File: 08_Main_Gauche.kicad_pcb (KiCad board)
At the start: 2 copper layers, 100 x 100 mm, 82 parts, among them J1 Conn_01x04, SW1 MX_1u, SW10 MX_1u, SW11 MX_1u, SW12 MX_1u, SW13 MX_1u, SW14 MX_1u, SW15 MX_1u, SW16 MX_1u, SW17 MX_1u, SW18 MX_1u, SW19 MX_1u, SW2 MX_1u, SW20 MX_1u, SW21 MX_1u, SW22 MX_1u, SW23 MX_1u, SW24 MX_1u, SW25 SW_Push, SW26 SW_Push, SW27 SW_Push, SW28 SW_Push, SW3 MX_1u, SW4 MX_1u, SW5 MX_1u, SW6 MX_1u, SW7 MX_1u, SW8 MX_1u, SW9 MX_1u, U1 MCP23017_SO

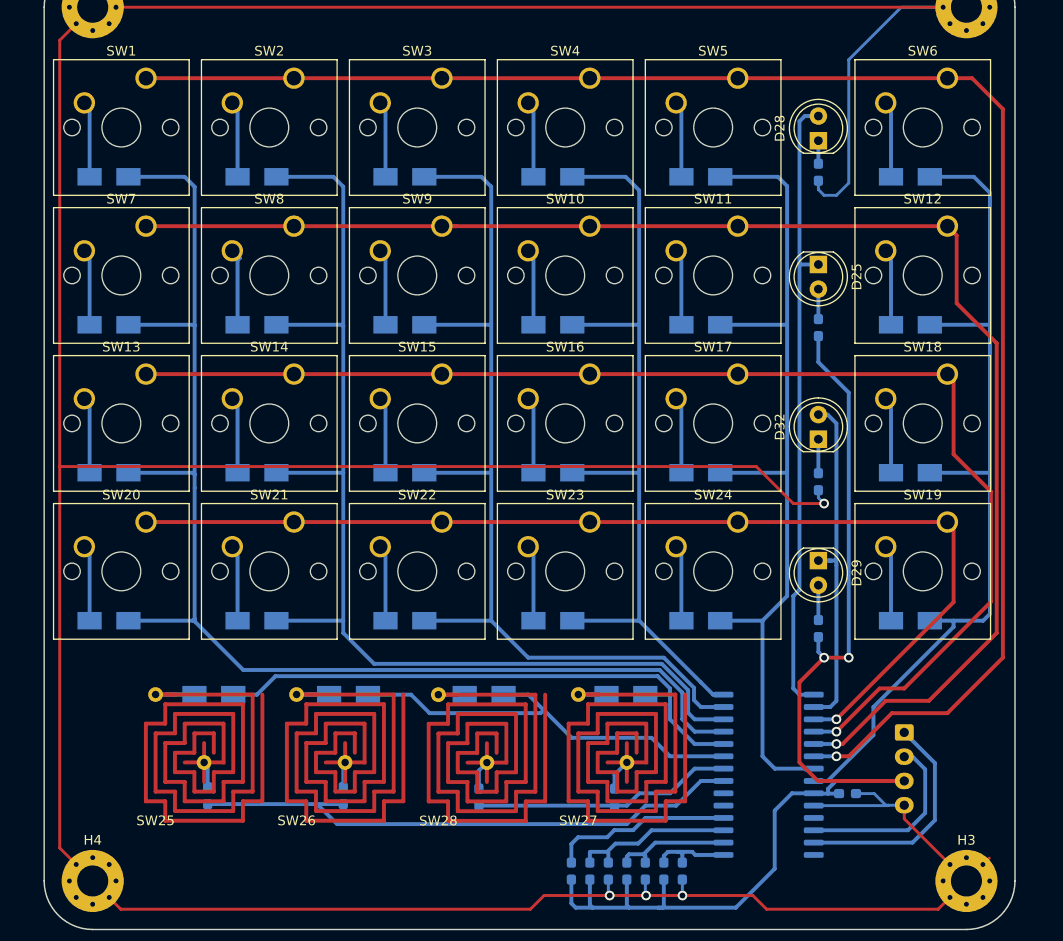
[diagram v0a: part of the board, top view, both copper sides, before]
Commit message: correction empreinte et routage; utilisation empreinte cherry mx led
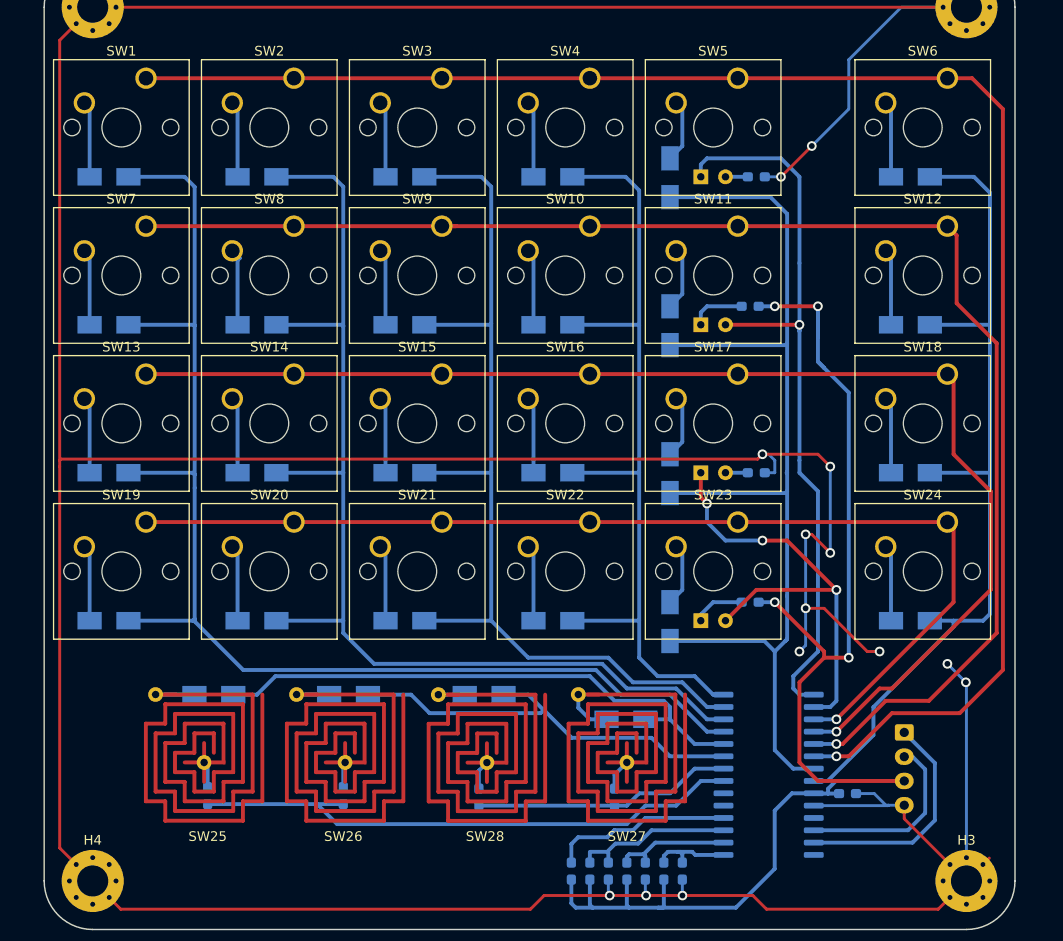
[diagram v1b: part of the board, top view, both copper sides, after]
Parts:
- removed D25, D28, D29, D32: LED, LED_THT:LED_D5.0mm
- removed the SW24 at (171.4, 113.0)
- added SW23: SW_Push_LED, Chimere:SW_MX_LED, F.Cu at (171.4, 113.0)
- SW11, SW17, SW5: value MX_1u -> SW_Push_LED; footprint Button_Switch_Keyboard:SW_Cherry_MX_1.00u_PCB -> Chimere:SW_MX_LED
- moved R7 7.54 mm to (172.7, 121.3), turned to 0 degrees
- moved R3 7.36 mm to (172.7, 90.8), turned to 0 degrees
- moved R9 6.46 mm to (173.4, 108.0), turned to 0 degrees
- moved R4 6.41 mm to (173.4, 77.5), turned to 0 degrees
- moved D11 3.18 mm to (164.5, 92.8), turned to 90 degrees
- moved D17 3.18 mm to (164.5, 108.0), turned to 90 degrees
- moved D23 3.18 mm to (164.5, 123.3), turned to 90 degrees
- moved D5 3.18 mm to (164.5, 77.6), turned to 90 degrees
- moved D30 2.54 mm to (159.9, 133.3)
- renumbered D20 to D19, D21 to D20, D22 to D21, D23 to D22, D24 to D23, D19 to D24, SW20 to SW19, SW21 to SW20, SW22 to SW21, SW23 to SW22, SW19 to SW24
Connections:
- R3 pad 1: Net-(D25-Pad2) -> Net-(R3-Pad1)
- R4 pad 1: Net-(D28-Pad1) -> Net-(R4-Pad1)
- R9 pad 1: Net-(D32-Pad1) -> Net-(R9-Pad1)
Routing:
- net GND: track 424.4 -> 482.8 mm, vias 4 -> 14
- net 3V3: track 119.5 -> 139.8 mm, vias 2 -> 4
- net COL1: track 91.0 -> 109.2 mm
- net LED1: track 35.7 -> 48.3 mm, vias 0 -> 3
- net LED0: track 65.2 -> 77.7 mm, vias 0 -> 1
- net Net-(R3-Pad1): track 0.00 -> 5.74 mm
- net Net-(D32-Pad1): track 3.50 -> 0.00 mm
- net Net-(D25-Pad2): track 3.08 -> 0.00 mm
- net Net-(D28-Pad1): track 2.38 -> 0.00 mm
- net Net-(R9-Pad1): track 0.00 -> 2.30 mm
- net Net-(R4-Pad1): track 0.00 -> 2.30 mm
- net COL2: track 84.4 -> 86.6 mm
- net Net-(D30-Pad2): track 2.91 -> 4.76 mm
- net Net-(R7-Pad1): track 3.58 -> 5.37 mm
- net COL5: track 133.4 -> 131.8 mm
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
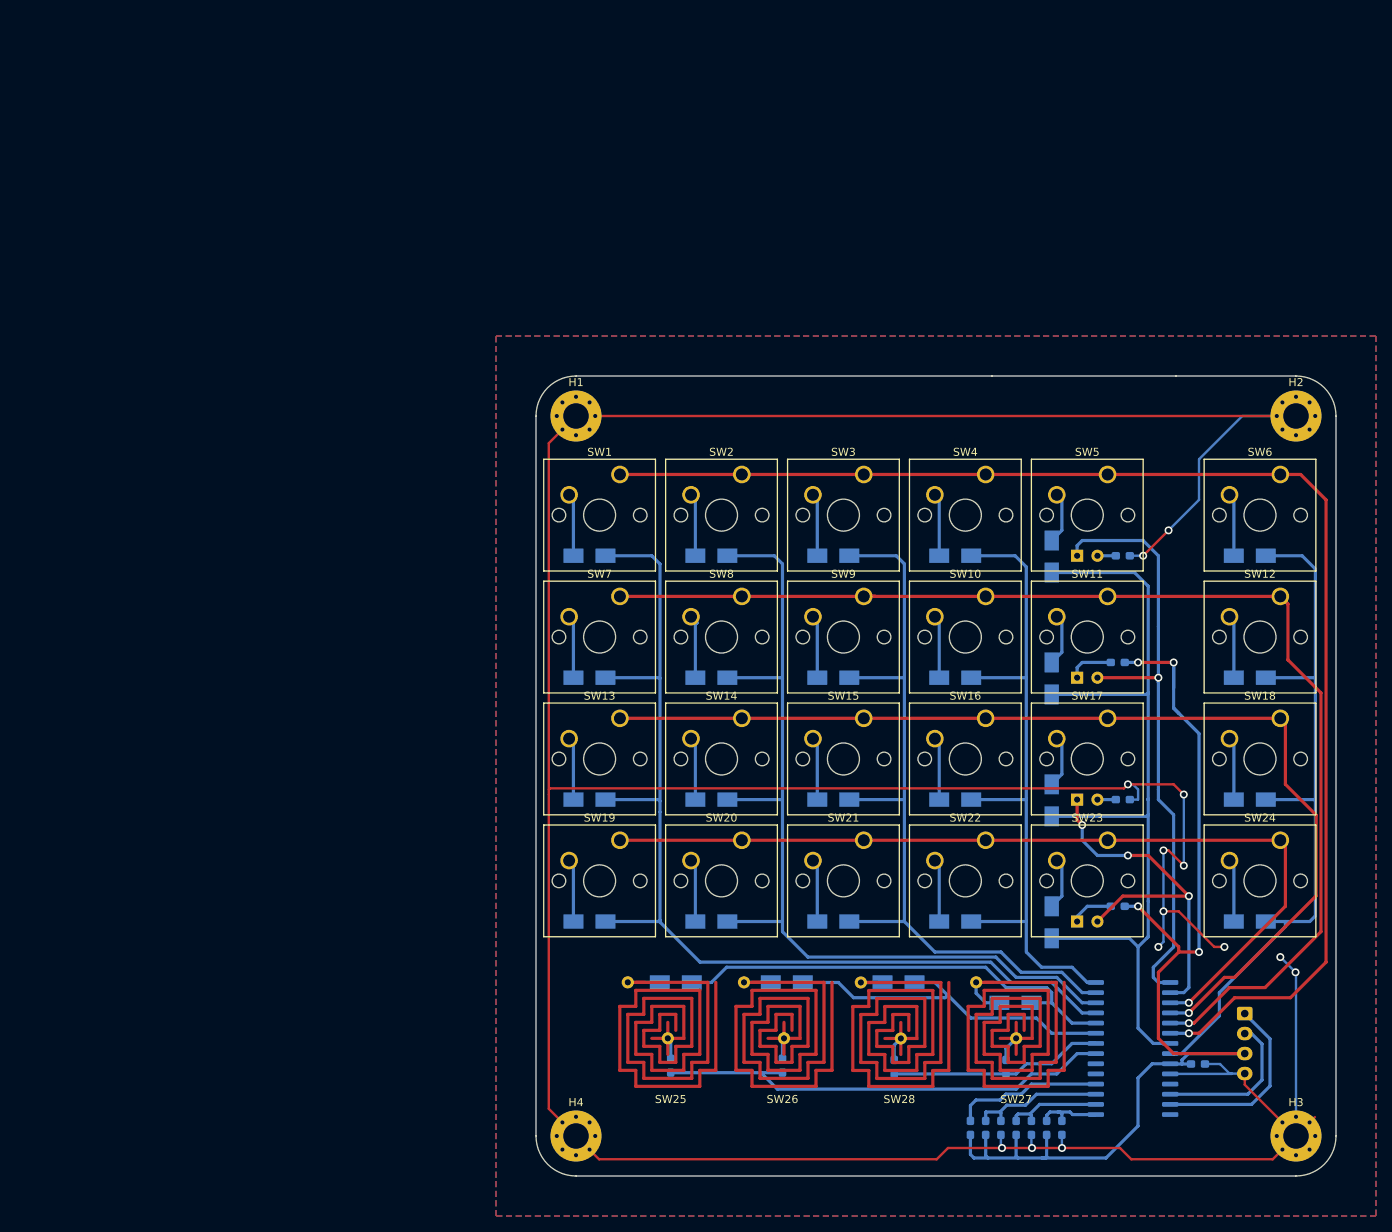
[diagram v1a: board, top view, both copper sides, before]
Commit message: schema + routage
- redistribution des touches
- ajout 5ways switch
- supprimé les empreintes pcb de touches résistives
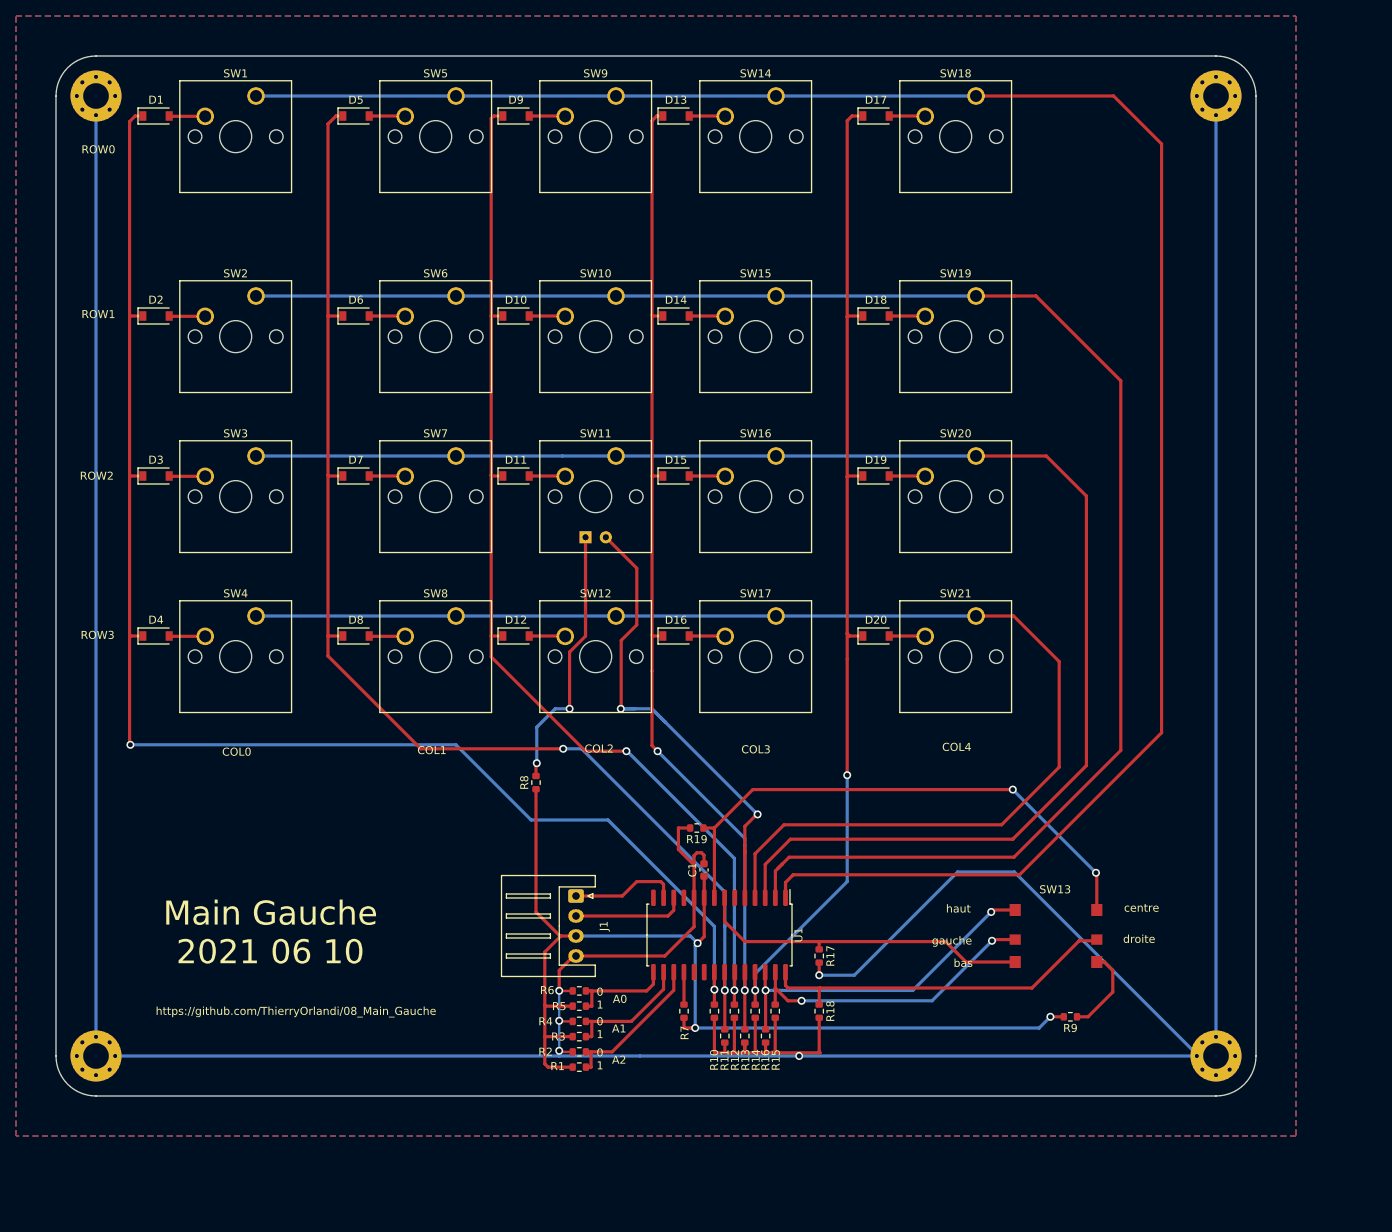
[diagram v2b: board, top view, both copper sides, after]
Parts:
- removed D21, D22, D23, D24, D26, D27, D30, D31: SS24, Diode_SMD:D_SMA
- removed the SW2 at (125.7, 67.3)
- removed SW22, SW24: MX_1u, Button_Switch_Keyboard:SW_Cherry_MX_1.00u_PCB
- removed SW23: SW_Push_LED, Chimere:SW_MX_LED
- removed SW25, SW26, SW27, SW28: SW_Push, Chimere:doigt_sw
- removed the SW3 at (141.0, 67.3)
- added R16: 100k, Resistor_SMD:R_0603_1608Metric, F.Cu at (128.7, 137.5)
- added R17: 100k, Resistor_SMD:R_0603_1608Metric, F.Cu at (135.4, 127.5)
- added R18: 100k, Resistor_SMD:R_0603_1608Metric, F.Cu at (135.4, 134.4)
- added R19: 100k, Resistor_SMD:R_0603_1608Metric, F.Cu at (120.1, 111.5)
- added SW12: MX_1u, Button_Switch_Keyboard:SW_Cherry_MX_1.00u_PCB, F.Cu at (110.0, 85.0)
- added SW18: MX_1u, Button_Switch_Keyboard:SW_Cherry_MX_1.00u_PCB, F.Cu at (155.0, 20.0)
- C1: footprint Capacitor_SMD:C_0603_1608Metric_Pad1.05x0.95mm_HandSolder -> Capacitor_SMD:C_0603_1608Metric; moved to F.Cu
- D1, D10, D11, D12, D13, D14, D15, D16, D17, D18, D19, D2, D20, D3, D4, D5, D6, D7, D8, D9: value SS24 -> B5819W; footprint Diode_SMD:D_SMA -> Diode_SMD:D_SOD-123; moved to F.Cu
- J1, U1: moved to F.Cu
- R1, R2, R5, R6: value 22M -> 100k; footprint Resistor_SMD:R_0603_1608Metric_Pad1.05x0.95mm_HandSolder -> Resistor_SMD:R_0603_1608Metric; moved to F.Cu
- R10, R11, R12, R13, R14, R15, R9: footprint Resistor_SMD:R_0603_1608Metric_Pad1.05x0.95mm_HandSolder -> Resistor_SMD:R_0603_1608Metric; moved to F.Cu
- R3, R4, R7: value 10k -> 100k; footprint Resistor_SMD:R_0603_1608Metric_Pad1.05x0.95mm_HandSolder -> Resistor_SMD:R_0603_1608Metric; moved to F.Cu
- R8: value 100k -> 10k; footprint Resistor_SMD:R_0603_1608Metric_Pad1.05x0.95mm_HandSolder -> Resistor_SMD:R_0603_1608Metric; moved to F.Cu
- SW13: value MX_1u -> K1-1506SN-01; footprint Button_Switch_Keyboard:SW_Cherry_MX_1.00u_PCB -> Chimere:K1-1506SN-01
- SW17, SW5: value SW_Push_LED -> MX_1u; footprint Chimere:SW_MX_LED -> Button_Switch_Keyboard:SW_Cherry_MX_1.00u_PCB
- moved SW2 133.4 mm to (65.0, 45.0)
- moved SW3 132.2 mm to (65.0, 65.0)
- moved D6 115.7 mm to (77.5, 47.5), turned to 0 degrees
- moved SW6 105.4 mm to (90.0, 45.0)
- moved D5 102.9 mm to (77.5, 22.5), turned to 0 degrees
- moved D4 100.4 mm to (52.5, 87.5), turned to 0 degrees
- moved SW5 94.2 mm to (90.0, 20.0)
- moved SW4 92.9 mm to (65.0, 85.0)
- moved D12 91.9 mm to (97.5, 87.5), turned to 0 degrees
- moved R4 89.5 mm to (105.4, 135.7)
- moved D17 88.3 mm to (142.5, 22.5), turned to 0 degrees
- moved D13 86.1 mm to (117.5, 22.5), turned to 0 degrees
- moved D3 85.2 mm to (52.5, 67.5), turned to 0 degrees
- moved J1 84.9 mm to (105.0, 120.0)
- moved R3 82.0 mm to (105.4, 137.6)
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- renumbered H3 to H2, H2 to H3, SW12 to SW2, SW18 to SW3
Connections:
- D1 pad 1: COL5 -> COL0
- D11 pad 1: COL1 -> COL2
- D12 pad 1: COL0 -> COL2
- D13 pad 1: COL5 -> COL3
- D14 pad 1: COL4 -> COL3
- D16 pad 1: COL2 -> COL3
- D17 pad 1: COL1 -> COL4
- D18 pad 1: COL0 -> COL4
- D19 pad 1: COL5 -> COL4
- D2 pad 1: COL4 -> COL0
- D3 pad 1: COL3 -> COL0
- D4 pad 1: COL2 -> COL0
- D6 pad 1: COL0 -> COL1
- D7 pad 1: COL5 -> COL1
- D8 pad 1: COL4 -> COL1
- D9 pad 1: COL3 -> COL2
- R1 pad 1: exp_row_1 -> 3V3
- R10 pad 1: 3V3 -> COL0
- R10 pad 2: Net-(R10-Pad2) -> GND
- R11 pad 1: GND -> COL1
- R11 pad 2: Net-(R10-Pad2) -> GND
- R12 pad 1: 3V3 -> COL2
- R12 pad 2: Net-(R12-Pad2) -> GND
- R13 pad 1: GND -> COL3
- R13 pad 2: Net-(R12-Pad2) -> GND
- R14 pad 1: 3V3 -> COL4
- R14 pad 2: Net-(R14-Pad2) -> GND
- R15 pad 1: GND -> gauche
- R15 pad 2: Net-(R14-Pad2) -> GND
- R2 pad 1: exp_row_1 -> GND
- R2 pad 2: Net-(R2-Pad2) -> Net-(R1-Pad2)
- R3 pad 1: Net-(R3-Pad1) -> 3V3
- R3 pad 2: 3V3 -> Net-(R3-Pad2)
- R4 pad 1: Net-(R4-Pad1) -> GND
- R4 pad 2: GND -> Net-(R3-Pad2)
- R5 pad 1: exp_row_0 -> 3V3
- R6 pad 1: exp_row_0 -> GND
- R6 pad 2: Net-(R6-Pad2) -> Net-(R5-Pad2)
- R7 pad 1: Net-(R7-Pad1) -> 3V3
- R7 pad 2: 3V3 -> Net-(R7-Pad2)
- R9 pad 2: GND -> 3V3
- SW1 pad 1: ROW3 -> ROW0
- SW10 pad 1: ROW2 -> ROW1
- SW11 pad 3: LED0 -> led
- SW11 pad 4: Net-(R3-Pad1) -> Net-(R8-Pad2)
- SW13 pad 1: ROW1 -> haut
- SW13 pad 2: Net-(D13-Pad2) -> gauche
- SW14 pad 1: ROW1 -> ROW0
- SW14 pad 2: Net-(D14-Pad2) -> Net-(D13-Pad2)
- SW15 pad 2: Net-(D15-Pad2) -> Net-(D14-Pad2)
- SW16 pad 1: ROW1 -> ROW2
- SW16 pad 2: Net-(D16-Pad2) -> Net-(D15-Pad2)
- SW17 pad 1: ROW1 -> ROW3
- SW17 pad 2: Net-(D17-Pad2) -> Net-(D16-Pad2)
- SW19 pad 1: ROW0 -> ROW1
- SW19 pad 2: Net-(D19-Pad2) -> Net-(D18-Pad2)
- SW2 pad 1: ROW2 -> ROW1
- SW2 pad 2: Net-(D12-Pad2) -> Net-(D2-Pad2)
- SW20 pad 1: ROW0 -> ROW2
- SW20 pad 2: Net-(D20-Pad2) -> Net-(D19-Pad2)
- SW21 pad 1: ROW0 -> ROW3
- SW21 pad 2: Net-(D21-Pad2) -> Net-(D20-Pad2)
- SW3 pad 1: ROW1 -> ROW2
- SW3 pad 2: Net-(D18-Pad2) -> Net-(D3-Pad2)
- SW5 pad 1: ROW3 -> ROW0
- SW6 pad 1: ROW3 -> ROW1
- SW8 pad 1: ROW2 -> ROW3
- SW9 pad 1: ROW2 -> ROW0
- U1 pad 1: LED0 -> ROW0
- U1 pad 15: Net-(R14-Pad2) -> Net-(R5-Pad2)
- U1 pad 16: Net-(R12-Pad2) -> Net-(R3-Pad2)
- U1 pad 17: Net-(R10-Pad2) -> Net-(R1-Pad2)
- U1 pad 18: Net-(R8-Pad2) -> Net-(R7-Pad2)
- U1 pad 2: LED1 -> ROW1
- U1 pad 21: exp_row_1 -> COL0
- U1 pad 22: exp_row_0 -> COL1
- U1 pad 23: exp_col_0 -> COL2
- U1 pad 24: exp_col_1 -> COL3
- U1 pad 25: COL5 -> COL4
- U1 pad 26: COL4 -> haut
- U1 pad 27: COL3 -> gauche
- U1 pad 28: COL2 -> droite
- U1 pad 3: ROW0 -> ROW2
- U1 pad 4: ROW1 -> ROW3
- U1 pad 5: ROW2 -> led
- U1 pad 6: ROW3 -> Net-(U1-Pad6)
- U1 pad 7: COL1 -> bas
- U1 pad 8: COL0 -> centre
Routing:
- net ROW0: track 110.5 -> 246.0 mm, vias 1 -> 0
- net COL5: track 131.8 -> 0.00 mm
- net COL0: track 92.4 -> 179.2 mm, vias 0 -> 2
- net ROW1: track 130.5 -> 212.3 mm, vias 1 -> 0
- net LED0: track 77.7 -> 0.00 mm, vias 1 -> 0
- net centre: track 0.00 -> 68.8 mm, vias 0 -> 2
- net led: track 0.00 -> 62.3 mm, vias 0 -> 2
- net exp_row_1: track 58.5 -> 0.00 mm
- net exp_col_1: track 57.5 -> 0.00 mm
- net GND: track 482.8 -> 539.6 mm, vias 14 -> 5
- net LED1: track 48.3 -> 0.00 mm, vias 3 -> 0
- net COL2: track 86.6 -> 134.7 mm, vias 0 -> 2
- net COL1: track 109.2 -> 155.6 mm, vias 0 -> 2
- net droite: track 0.00 -> 45.3 mm
- net exp_col_0: track 44.3 -> 0.00 mm
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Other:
- board size 100 x 100 mm -> 150 x 130 mm
- board text added: "0 1"
- board text added: "A0"
- board text added: "A1"
- board text added: "A2"
- board text added: "COL0"
- board text added: "COL1"
- board text added: "COL2"
- board text added: "COL3"
- board text added: "COL4"
- board text added: "Main Gauche 2021 06 10"
- board text added: "ROW0"
- board text added: "ROW1"
- board text added: "ROW2"
- board text added: "ROW3"
- board text added: "bas"
- board text added: "centre"
- board text added: "droite"
- board text added: "gauche"
- board text added: "haut"
- board text removed: "Main Gauche 2021 04 11"
